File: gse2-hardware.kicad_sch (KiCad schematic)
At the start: 61 parts, among them J1 PJ-002A, J16 ARM, J17 ALARM, J2 PJ-002A, J3 ARM Cortex Debug, J4 USB-C, Q1 DMP3099L, Q15 DMG3402L, U27 USBLC6-2SC6, Y1 16MHz

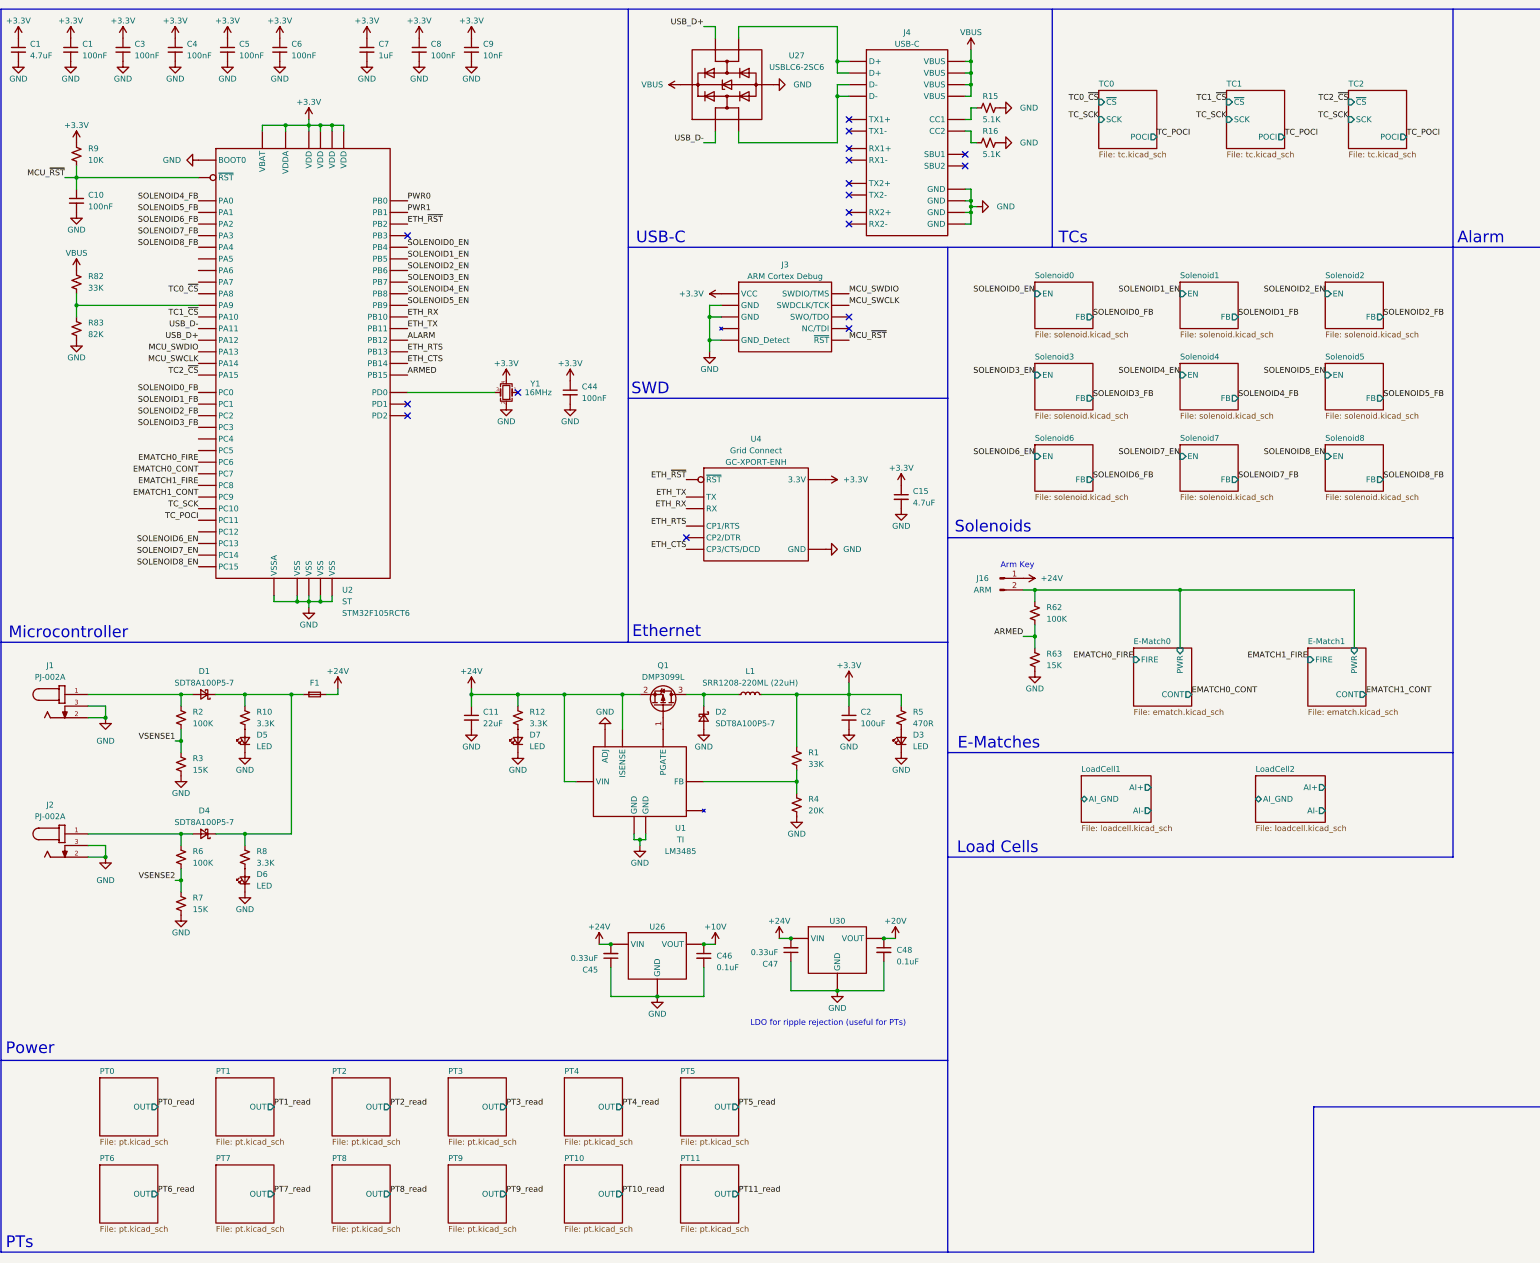
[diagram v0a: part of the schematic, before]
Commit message: Updated schematic. No filtering but besides that finished. Need to fix footprints and start layout.
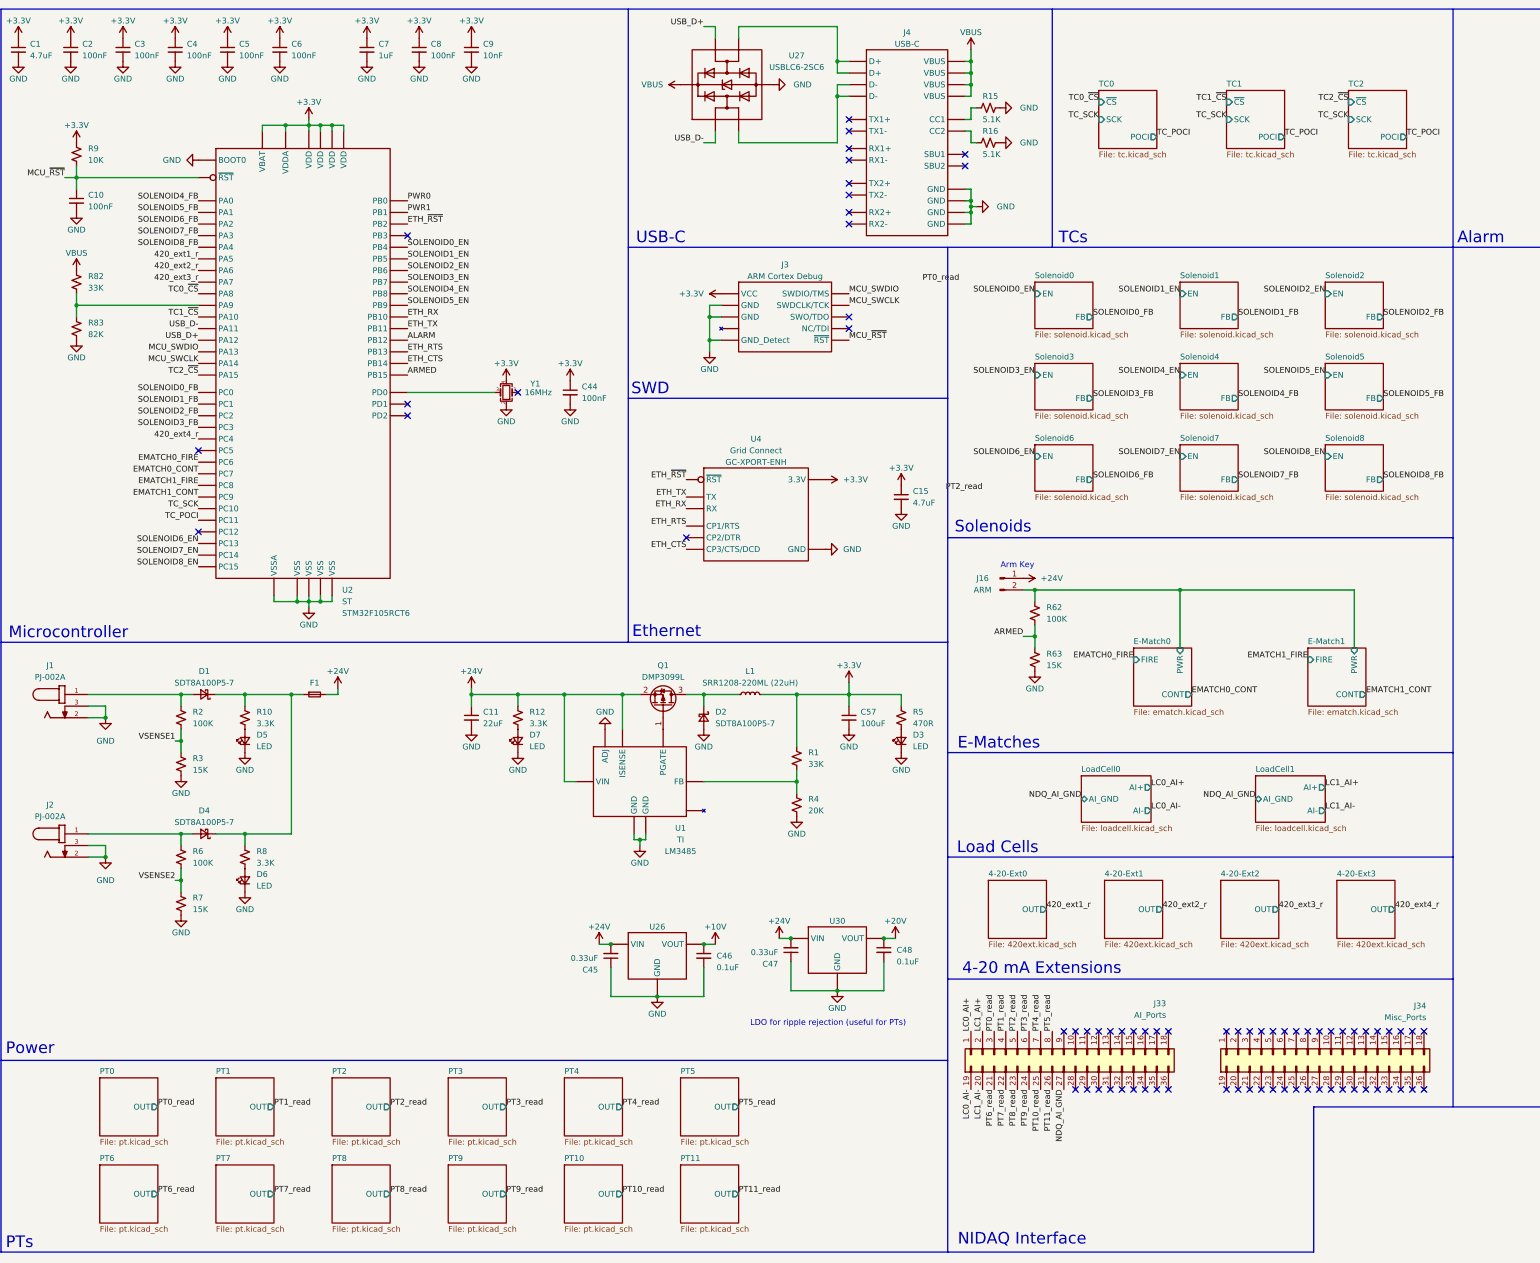
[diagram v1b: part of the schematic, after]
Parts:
- removed C2: 100uF, Capacitor_SMD:C_1206_3216Metric, symbol Device:C_Small
- added C57: 100uF, Capacitor_SMD:C_1206_3216Metric, symbol Device:C_Small
- added J33: AI_Ports, symbol Connector_Generic:Conn_02x18_Top_Bottom
- added J34: Misc_Ports, symbol Connector_Generic:Conn_02x18_Top_Bottom
- U1: footprint Package_SO:VSSOP-8_3.0x3.0mm_P0.65mm -> Package_SO:VSSOP-8_3x3mm_P0.65mm
- U4: footprint UCIRP-KiCAD-Lib:GC-XPORT -> 0UCIRP-KiCAD-Lib:GC-XPORT
- renumbered C1 to C2
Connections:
- net +3.3V: now also C57.1
- net GND: now also C57.2
- net PT0_read: now also J33.3 (Pin_3)
- net PT10_read: now also J33.25 (Pin_25)
- net PT11_read: now also J33.26 (Pin_26)
- net PT1_read: now also J33.4 (Pin_4)
- net PT2_read: now also J33.5 (Pin_5)
- net PT3_read: now also J33.6 (Pin_6)
- net PT4_read: now also J33.7 (Pin_7)
- net PT5_read: now also J33.8 (Pin_8)
- net PT6_read: now also J33.21 (Pin_21)
- net PT7_read: now also J33.22 (Pin_22)
- net PT8_read: now also J33.23 (Pin_23)
- net PT9_read: now also J33.24 (Pin_24)
- net 420_ext1_r: now reaches U2.21 (PA5)
- net 420_ext2_r: now reaches U2.22 (PA6)
- net 420_ext3_r: now reaches U2.23 (PA7)
- net 420_ext4_r: now reaches U2.24 (PC4)
- new net LC0_AI+: J33.1 (Pin_1)
- new net LC0_AI-: J33.19 (Pin_19)
- new net LC1_AI+: J33.2 (Pin_2)
- new net LC1_AI-: J33.20 (Pin_20)
- new net NDQ_AI_GND: J33.27 (Pin_27)
- no-connect marks 17 -> 74
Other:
- removed sheet LoadCell2
- added sheet 4-20-Ext0 (420ext.kicad_sch)
- added sheet 4-20-Ext1 (420ext.kicad_sch)
- added sheet 4-20-Ext2 (420ext.kicad_sch)
- added sheet 4-20-Ext3 (420ext.kicad_sch)
- added sheet LoadCell0 (loadcell.kicad_sch)
- note added: "4-20 mA Extensions"
- note added: "NIDAQ Interface"

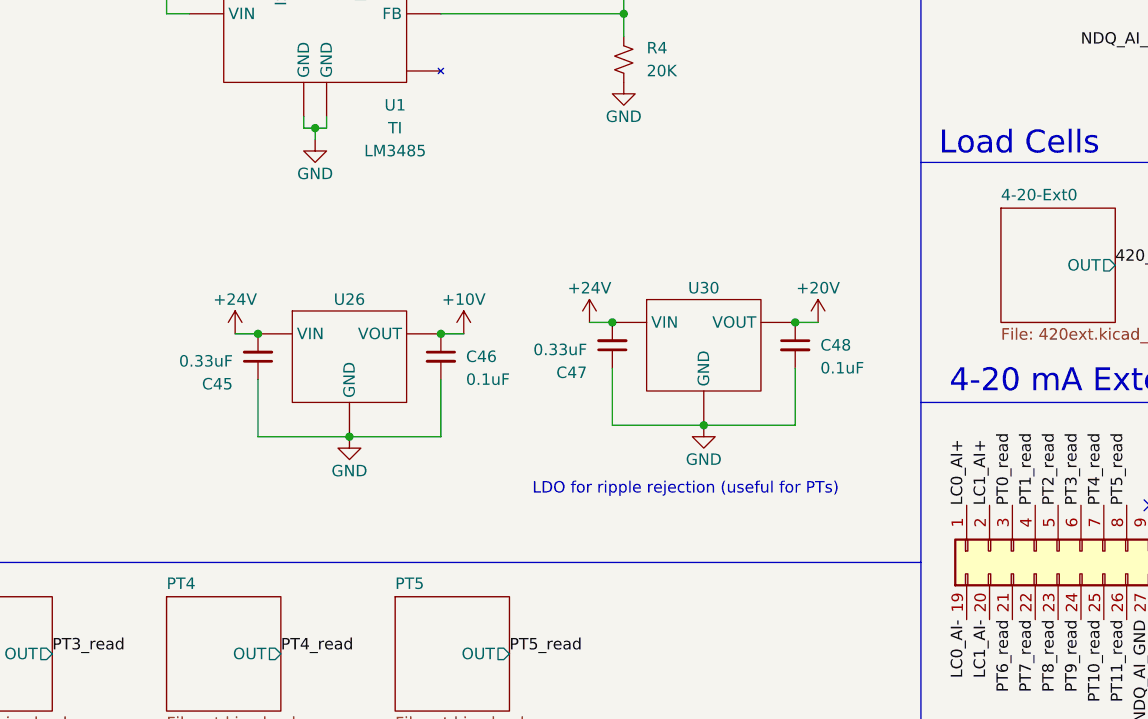
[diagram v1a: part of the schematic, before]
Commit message: Added LC filter for power filtering
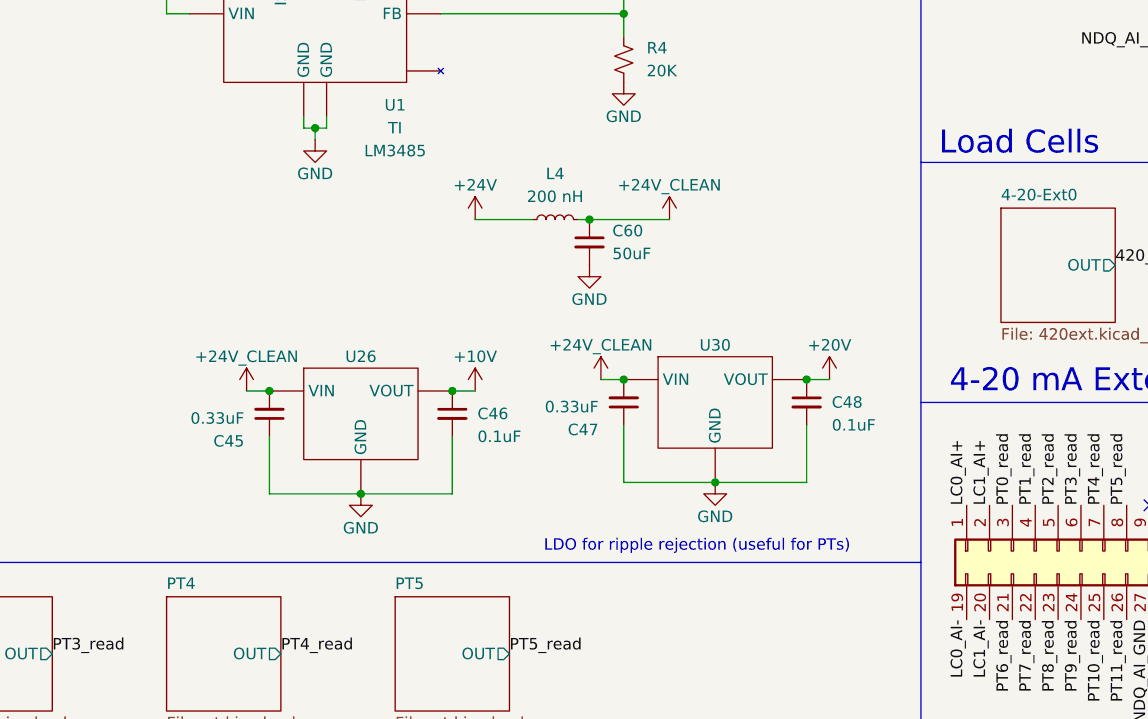
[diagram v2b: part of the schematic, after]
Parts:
- added C60: 50uF, Capacitor_SMD:C_1206_3216Metric, symbol Device:C_Small
- added L4: 200 nH, Inductor_SMD:L_Bourns_SRR1208_12.7x12.7mm, symbol Device:L_Small
- J16, J17: footprint TerminalBlock:TerminalBlock_bornier-2_P5.08mm -> TerminalBlock_MetzConnect:TerminalBlock_MetzConnect_Type055_RT01502HDWU_1x02_P5.00mm_Horizontal
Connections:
- net +24V: now also L4.1; no longer C45.2, C47.2, U26.1 (VIN), U30.1 (VIN)
- net GND: now also C60.2
- new net +24V_CLEAN: C45.2, C47.2, C60.1, L4.2, U26.1 (VIN), U30.1 (VIN)
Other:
- moved on the sheet: C45, C46, C47, C48, U26, U30

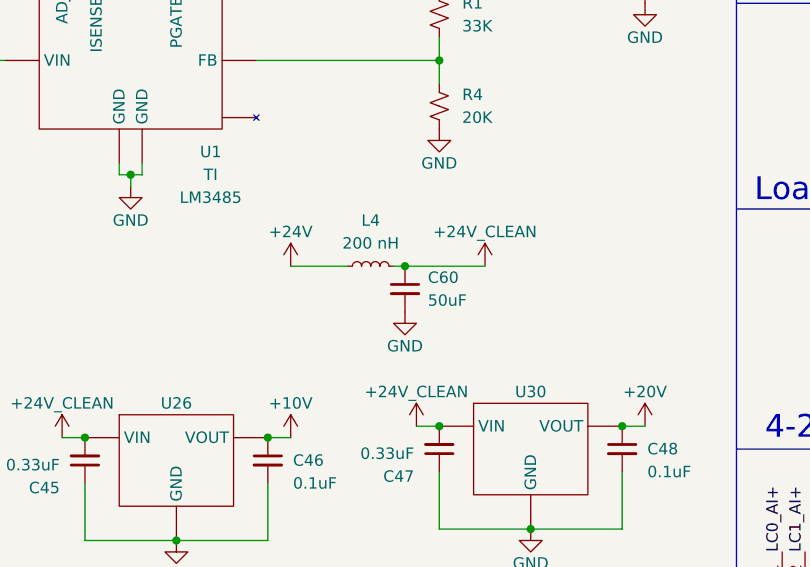
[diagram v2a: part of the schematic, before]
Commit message: Removed extra filtering circuit
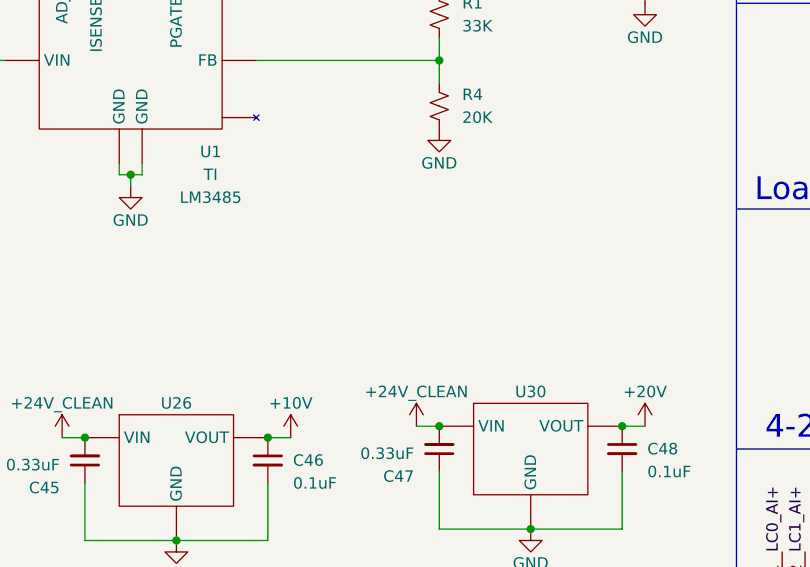
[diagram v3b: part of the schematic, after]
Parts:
- removed C60: 50uF, Capacitor_SMD:C_1206_3216Metric, symbol Device:C_Small
- removed L4: 200 nH, Inductor_SMD:L_Bourns_SRR1208_12.7x12.7mm, symbol Device:L_Small

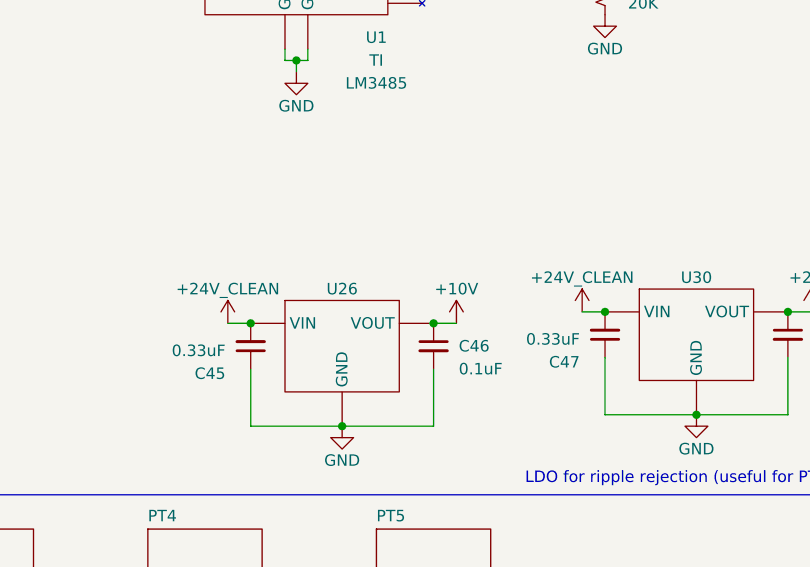
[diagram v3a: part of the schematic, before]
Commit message: Fixed net names
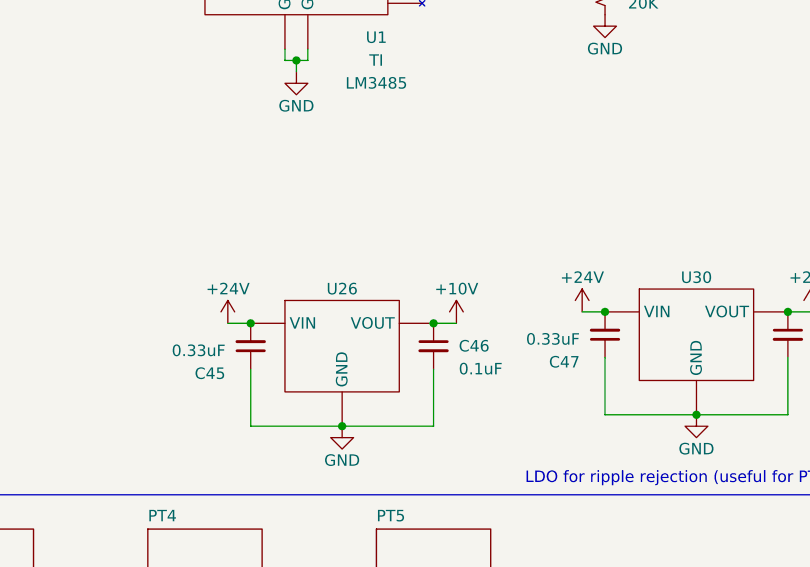
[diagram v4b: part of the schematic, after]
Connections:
- net +24V_CLEAN is gone; now on net +24V: C45.2, C47.2, U26.1 (VIN), U30.1 (VIN)
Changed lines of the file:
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@@
 			)
 		)
-		(property "Value" "+24V_CLEAN"
+		(property "Value" "+24V"
 			(at 144.78 219.71 0)
 			(effects
@@
 			)
 		)
-		(property "Value" "+24V_CLEAN"
+		(property "Value" "+24V"
 			(at 184.15 218.44 0)
 			(effects

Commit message: Updates after PDR
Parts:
- removed R2, R6: 100K, Resistor_SMD:R_0402_1005Metric, symbol Device:R_Small_US
- removed R3, R7: 15K, Resistor_SMD:R_0402_1005Metric, symbol Device:R_Small_US
- added C50: 0.33uF, Capacitor_SMD:C_1206_3216Metric, symbol Device:C_Small
- added C51: 0.1uF, Capacitor_SMD:C_1206_3216Metric, symbol Device:C_Small
- added U35: ~, Package_TO_SOT_SMD:TO-252-2, symbol UCIRP-KiCAD-Lib:Generic_Regulator_InputGroundOutput
- U30: Part # (none) -> BA78M20FP-E2
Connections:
- net NDQ_AI_GND is gone; now on net GND: J33.27 (Pin_27)
- net +24V: now also C50.2, U35.1 (VIN)
- net GND: now also C50.1, C51.2, U35.2 (GND)
- net V_SENSE3: now reaches U2.25 (PC5)
- net 420_ext4_r renamed V_SENSE2
- net PWR0 renamed V_SENSE0
- net PWR1 renamed V_SENSE1
- new net +10V_LOAD_CELL: C51.1, U35.3 (VOUT)
- no-connect marks 74 -> 73
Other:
- removed sheet 4-20-Ext3
- added sheet Volt-Sense0 (voltsense.kicad_sch)
- added sheet Volt-Sense1 (voltsense.kicad_sch)
- added sheet Volt-Sense2 (voltsense.kicad_sch)
- added sheet Volt-Sense3 (voltsense.kicad_sch)
- note added: "For PTs, based on https://www.ni.com/en/shop/data-acquisition/measurement -fundamentals/field-wiring-and-noise-considerations-for-analog-signals.html"
- moved on the sheet: D1, D4, D5, D6, F1, R10, R8

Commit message: Updated to add new filtering circuit
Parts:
- removed C50: 0.33uF, Capacitor_SMD:C_1206_3216Metric, symbol Device:C_Small
- removed C51: 0.1uF, Capacitor_SMD:C_1206_3216Metric, symbol Device:C_Small
- removed U35: ~, Package_TO_SOT_SMD:TO-252-2, symbol UCIRP-KiCAD-Lib:Generic_Regulator_InputGroundOutput
- added C69: 0.33uF, Capacitor_SMD:C_1206_3216Metric, symbol Device:C_Small
- added C70: 0.1uF, Capacitor_SMD:C_1206_3216Metric, symbol Device:C_Small
- added R104, R2: 15K, Resistor_SMD:R_0402_1005Metric, symbol Device:R_Small_US
- added R2, R7: 100K, Resistor_SMD:R_0402_1005Metric, symbol Device:R_Small_US
- added U33: ~, Package_TO_SOT_SMD:SOT-89-3, symbol UCIRP-KiCAD-Lib:Generic_Regulator_InputGroundOutput
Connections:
- net 420_ext1_r is gone; now on net V_SENSE0: U2.21 (PA5)
- net 420_ext2_r is gone; now on net V_SENSE1: U2.22 (PA6)
- net 420_ext3_r is gone; now on net V_SENSE2: U2.23 (PA7)
- net +24V: now also C69.2, U33.1 (VIN)
- net GND: now also C69.1, C70.2, R104.1, R2.1, U33.2 (GND)
- net V_SENSE0: no longer U2.26 (PB0)
- net V_SENSE1: no longer U2.27 (PB1)
- net V_SENSE2: no longer U2.24 (PC4)
- net V_SENSE3: now also U2.24 (PC4); no longer U2.25 (PC5)
- net at D1.2 (A), J1.1: now also R2.2
- net at D4.2 (A), J2.1: now also R7.2
- new net +5V: C70.1, U33.3 (VOUT)
- new net PWR0: R2.1, R2.2, U2.26 (PB0)
- new net PWR1: R104.2, R7.1, U2.27 (PB1)
- new net V_SENSE4: U2.25 (PC5)
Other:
- removed sheet 4-20-Ext0
- removed sheet 4-20-Ext1
- removed sheet 4-20-Ext2
- added sheet Volt-Sense4 (voltsense.kicad_sch)
- note added: "Voltage Sensing"
- note removed: "4-20 mA Extensions"
- note removed: "LDO for ripple rejection (useful for PTs)"
- moved on the sheet: C11, C44, C45, C46, C47, C48, C57, D1, D2, D3, D4, D5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
